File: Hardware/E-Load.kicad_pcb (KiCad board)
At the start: 2 copper layers, 63.5 x 71.1 mm, 56 parts, among them J1 PJ-002A, J2 Conn_01x05_Male, J3 Conn_01x08_Male, J4 Screw_Terminal_01x03, Q1 BUK7M45-40EX, SW2 SW_Push, SW3 SW_Push, SW4 SW_Push, U1 AP2210K-3.3, U2 STM32F103C8Tx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

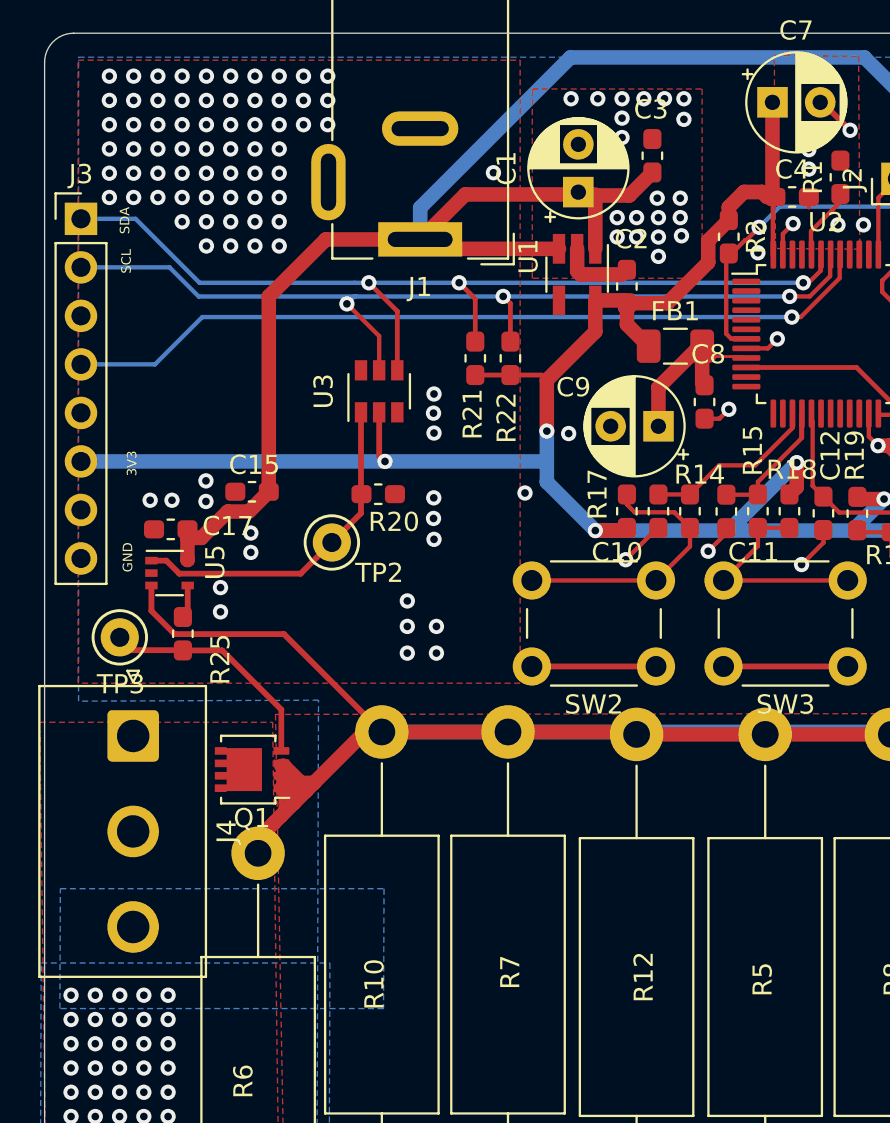
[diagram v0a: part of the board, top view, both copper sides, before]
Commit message: updated C1 footprint, updated MCU schematic. Fixed possible issue with buttons
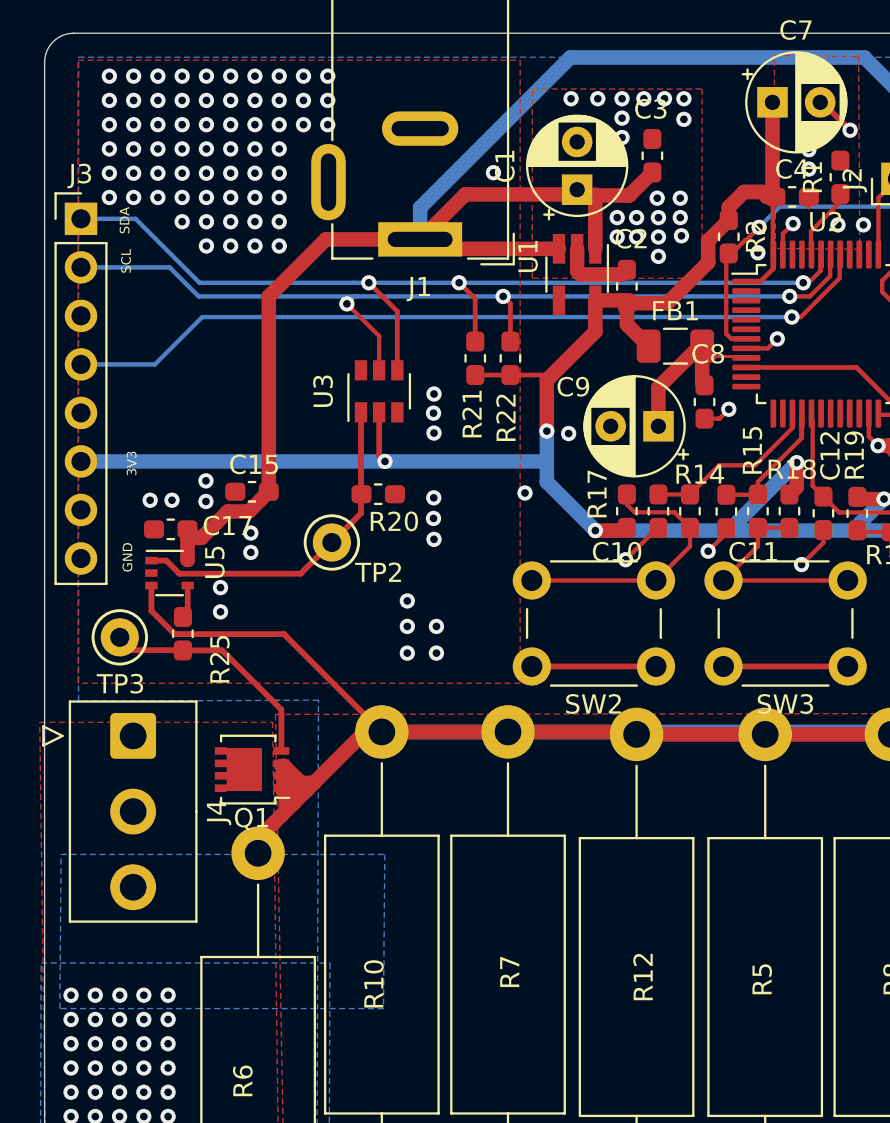
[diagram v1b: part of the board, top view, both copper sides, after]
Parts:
- J4: footprint Connector_JST:JST_NV_B03P-NV_1x03_P5.00mm_Vertical -> Connector_TE-Connectivity:TE_826576-3_1x03_P3.96mm_Vertical
- moved C1 0.14 mm to (170.1, 67.6)
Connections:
- U2 pad 1: (no net) -> +3V3
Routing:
- net +3V3: track 140.6 -> 143.0 mm

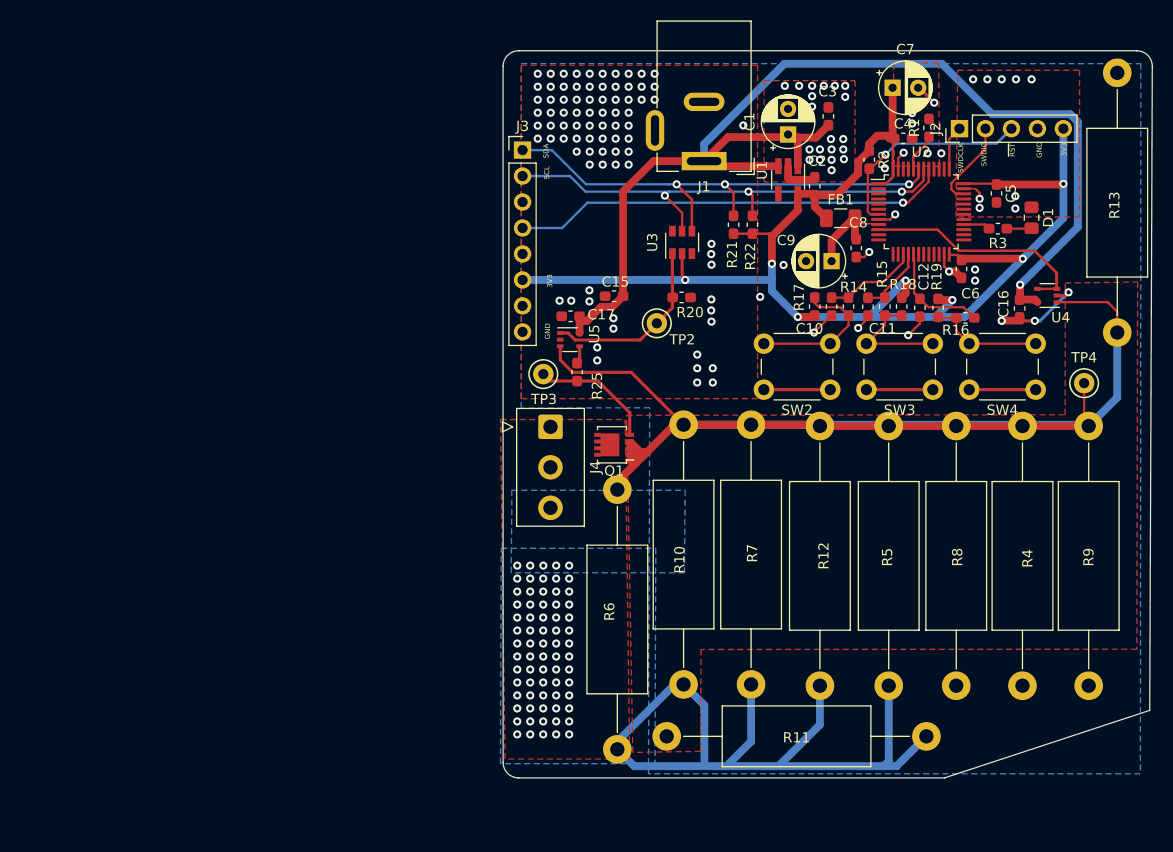
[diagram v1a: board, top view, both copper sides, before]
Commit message: Added new FET and opamp. Repositioned parts on PCB
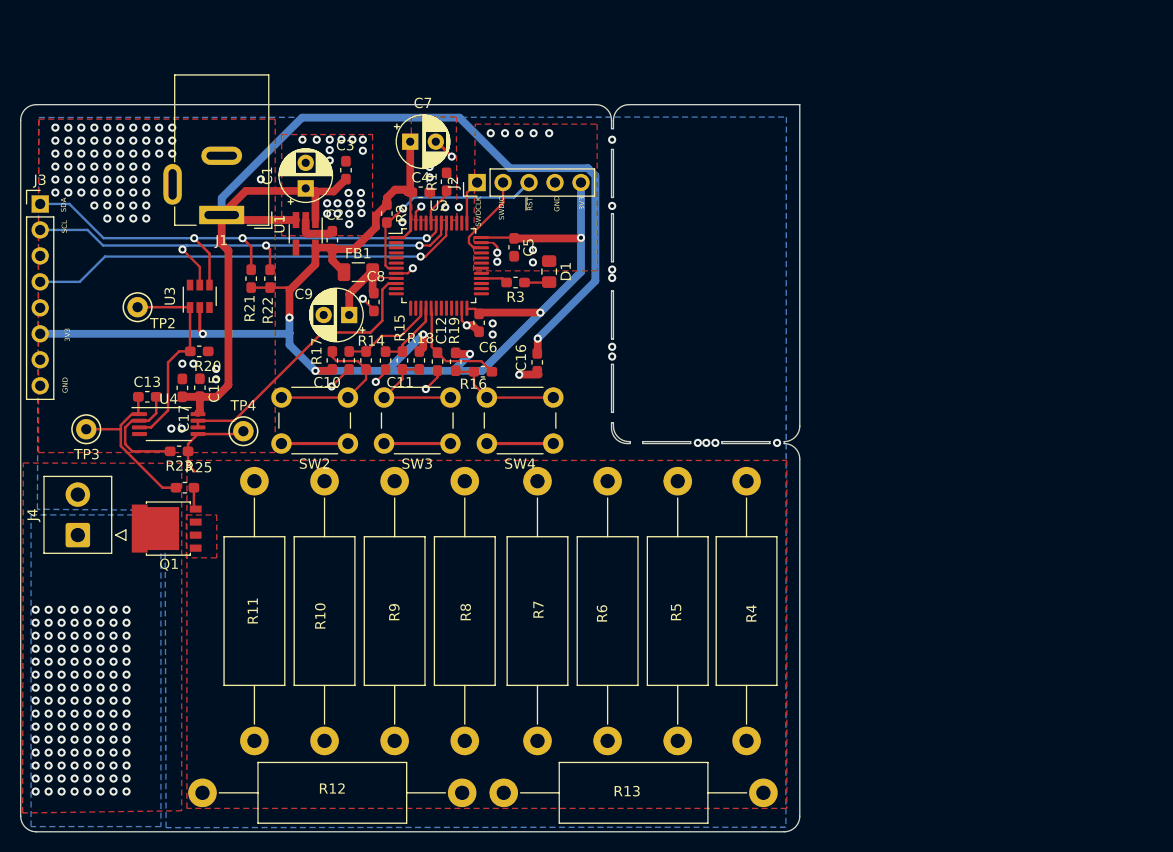
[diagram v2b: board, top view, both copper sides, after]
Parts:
- removed U5: TLV172IDCK, Package_TO_SOT_SMD:SOT-353_SC-70-5
- added C13: 470p, Capacitor_SMD:C_0603_1608Metric_Pad1.05x0.95mm_HandSolder, F.Cu at (107.4, 93.3)
- added R23: 1k, Resistor_SMD:R_0603_1608Metric_Pad1.05x0.95mm_HandSolder, F.Cu at (110.6, 98.6)
- J4: value Screw_Terminal_01x03 -> Screw_Terminal_01x02; footprint Connector_TE-Connectivity:TE_826576-3_1x03_P3.96mm_Vertical -> Connector_TE-Connectivity:TE_826576-2_1x02_P3.96mm_Vertical
- Q1: value BUK7M45-40EX -> PSMN5R2-60YL; footprint Package_TO_SOT_SMD:LFPAK33 -> Package_TO_SOT_SMD:LFPAK56
- U4: value TLV172IDCK -> TLV9102IPWR; footprint Package_TO_SOT_SMD:SOT-353_SC-70-5 -> Package_SO:TSSOP-8_4.4x3mm_P0.65mm
- moved U4 86.8 mm to (109.5, 95.9), turned to 0 degrees
- moved TP4 82.4 mm to (116.8, 96.6)
- moved R12 70.2 mm to (112.8, 132.0), turned to 0 degrees
- moved R9 68.1 mm to (131.6, 101.5)
- moved R13 56.8 mm to (167.7, 132.0), turned to 180 degrees
- moved TP2 50.8 mm to (106.5, 84.5)
- moved R8 48.4 mm to (138.5, 101.5)
- moved C16 47.5 mm to (145.6, 89.9)
- moved J2 47.5 mm to (139.7, 72.3)
- moved R16 47.5 mm to (140.3, 90.8)
- moved R18 47.5 mm to (134.0, 89.7)
- moved C10 47.5 mm to (127.2, 89.7)
- moved C3 47.5 mm to (126.9, 71.1)
- moved C9 47.5 mm to (127.2, 85.3)
- moved J3 47.5 mm to (97.0, 74.4)
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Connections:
- J4 pad 2: (no net) -> GND
- R25 pad 2: Net-(R25-Pad2) -> Net-(C13-Pad1)
- TP3 pad 1: Net-(Q1-Pad4) -> Net-(C13-Pad1)
- U4 pad 1: /CurrentControl/Vmeas -> Net-(C13-Pad1)
- U4 pad 2: GND -> Net-(C13-Pad2)
- U4 pad 3: /CurrentControl/ADC -> Net-(R20-Pad2)
- U4 pad 4: /CurrentControl/ADC -> GND
- U4 pad 5: +12V -> /CurrentControl/Vmeas
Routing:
- net /CurrentControl/Vmeas: track 135.7 -> 8.89 mm
- net GND: track 130.4 -> 46.0 mm, vias 132 -> 125
- net Net-(C13-Pad1): track 0.00 -> 16.5 mm
- net Net-(C13-Pad2): track 0.00 -> 11.5 mm
- net Net-(Q1-Pad4): track 12.0 -> 2.16 mm
- net /CurrentControl/ADC: track 22.6 -> 27.4 mm
- net +12V: track 116.0 -> 111.9 mm
- net Net-(R20-Pad2): track 17.8 -> 20.2 mm
- net Net-(R25-Pad2): track 1.75 -> 0.00 mm
- net VCC: vias 70 -> 120
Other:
- board size 63.5 x 71.1 mm -> 76.2 x 71.1 mm
